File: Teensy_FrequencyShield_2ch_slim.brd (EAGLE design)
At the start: 40.6 x 83.8 mm, 10 parts

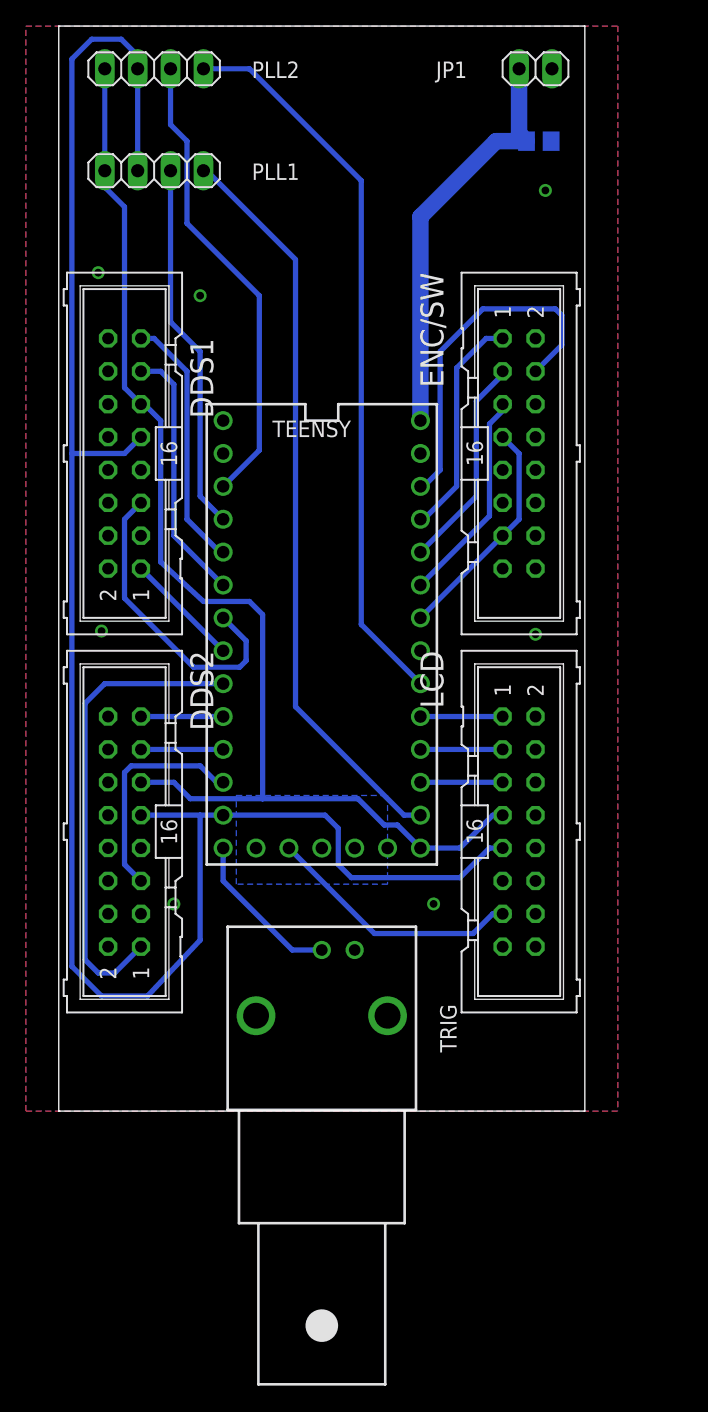
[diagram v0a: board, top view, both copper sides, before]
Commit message: Updated 2ch teensy frequency breakout
* uses 8-pin LCD and encoder headers
* other changes possible...
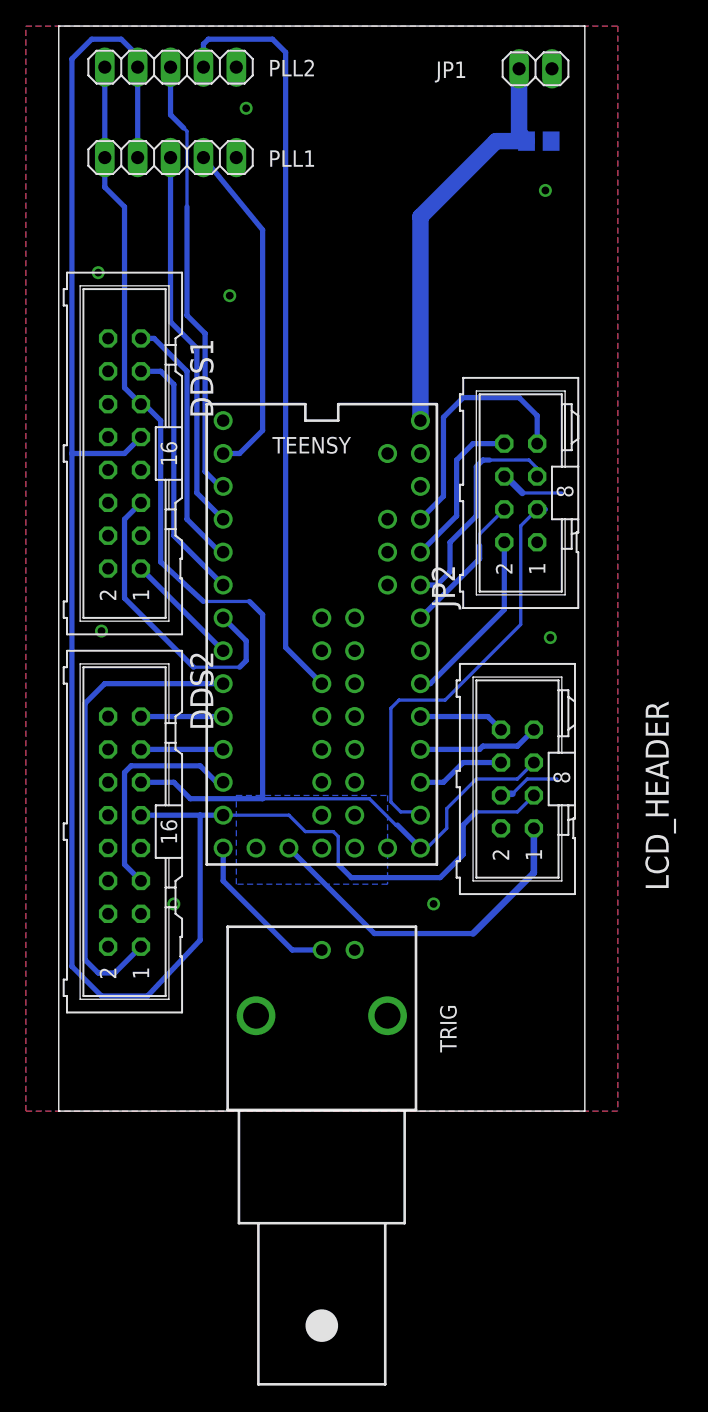
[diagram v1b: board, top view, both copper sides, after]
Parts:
- removed ENC/SW, LCD: (no value), mcu-accessories:ML16
- added JP2, LCD_HEADER: (no value), mcu-accessories:ML08
- PLL1, PLL2: device pinhead:1X04 -> pinhead:1X05
- TEENSY: value TEENSY_3.1_BASIC -> TEENSY_3.1_ALL_PINS_AND_PADS; device mcu-accessories:TEENSY_3.1_BASIC -> mcu-accessories:TEENSY_3.1_ALLPINS
- moved PLL1 1.63 mm to (-34.5, 43.2)
- moved PLL2 1.28 mm to (-34.5, 50.2)
- moved TEENSY 1.27 mm to (-22.9, 5.08)
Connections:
- removed net ENC_A: ENC/SW.7, TEENSY.20/A6
- removed net ENC_B: ENC/SW.5, TEENSY.21/A7
- removed net ENC_SW: ENC/SW.1, TEENSY.23/A9
- removed net SW1: ENC/SW.3, TEENSY.22/A8
- removed net VDD: ENC/SW.4, LCD.13, TEENSY.3.3V, TEENSY.3.3V1
- new net AREF: TEENSY.AREF
- new net ENC_A1: JP2.5, TEENSY.21/A7
- new net ENC_A2: JP2.3, TEENSY.14/A0
- new net ENC_B1: JP2.7, TEENSY.23/A9
- new net ENC_B2: JP2.4, TEENSY.20/A6
- new net ENC_SW1: JP2.8, TEENSY.22/A8
- new net ENC_SW2: JP2.2, TEENSY.18/A4
- new net EROU: LCD_HEADER.1, TEENSY.3.3V, TEENSY.3.3V1, TEENSY.3.3V2
- new net VUSB: TEENSY.VUSB
- net CLK: now also LCD_HEADER.5; no longer LCD.7
- net GND: now also JP2.1, JP2.6, LCD_HEADER.2, LCD_HEADER.4, PLL1.5, PLL2.5, TEENSY.GND2; no longer ENC/SW.15, LCD.11
- net LCD_CSB: now also LCD_HEADER.6; no longer LCD.5
- net LCD_RS: now also LCD_HEADER.7; no longer LCD.3
- net LCD_RST: now also LCD_HEADER.8; no longer LCD.1
- net MOSI: now also LCD_HEADER.3; no longer LCD.9
- net PLL1_MUX: now also TEENSY.0; no longer TEENSY.14/A0
- net PLL2_MUX: now also TEENSY.24; no longer TEENSY.18/A4
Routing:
- net VDD: track 47.7 -> 0.00 mm
- net ENC_A2: track 0.00 -> 32.7 mm
- net PLL1_MUX: track 57.6 -> 26.5 mm
- net EROU: track 0.00 -> 27.0 mm
- net ENC_B1: track 0.00 -> 19.2 mm
- net ENC_A1: track 0.00 -> 17.7 mm
- net ENC_A: track 17.7 -> 0.00 mm
- net ENC_SW: track 17.5 -> 0.00 mm
- net ENC_B: track 17.3 -> 0.00 mm
- net SW1: track 17.0 -> 0.00 mm
- net ENC_SW2: track 0.00 -> 14.1 mm
- net ENC_SW1: track 0.00 -> 12.5 mm
- net ENC_B2: track 0.00 -> 11.1 mm
- net GND: track 0.00 -> 9.40 mm, vias 7 -> 8
- net CLK: track 94.8 -> 100.0 mm
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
